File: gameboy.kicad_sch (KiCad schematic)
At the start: 0 parts

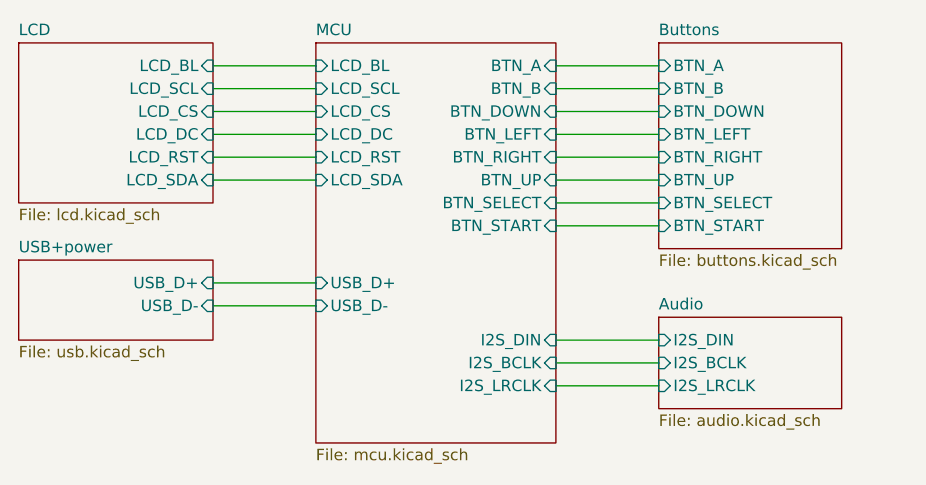
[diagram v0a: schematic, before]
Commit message: add amplifier mode selector, add drawing lcd
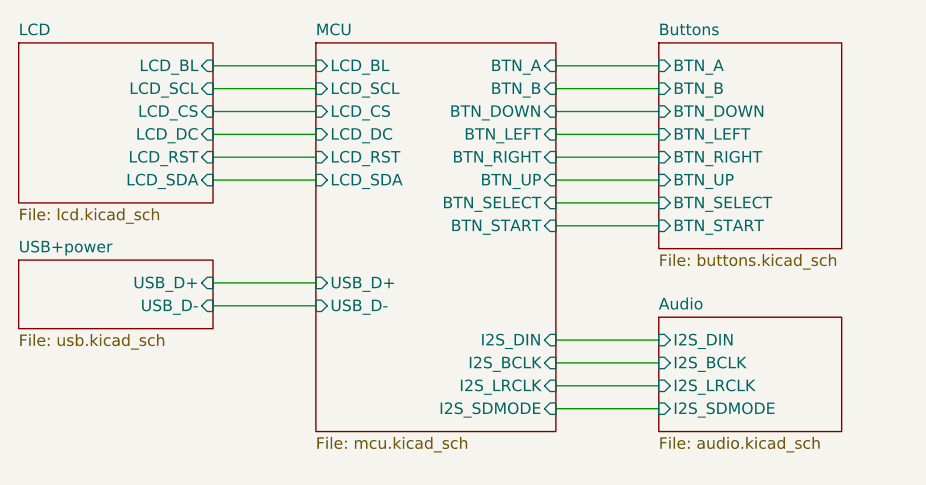
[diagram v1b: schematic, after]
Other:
- sheet Audio ports: added I2S_SDMODE; removed none
- sheet MCU ports: added I2S_SDMODE; removed none
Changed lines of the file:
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@@
+	(wire
+		(pts
+			(xy 167.64 99.06) (xy 179.07 99.06)
+		)
+		(stroke
+			(width 0)
+			(type default)
+		)
+	)
 	(wire
 		(pts
@@
 	(sheet
 		(at 140.97 58.42)
-		(size 26.67 44.45)
+		(size 26.67 43.18)
 		(exclude_from_sim no)
 		(in_bom yes)
@@
 		)
 		(property "Sheetfile" "mcu.kicad_sch"
-			(at 140.97 103.4546 0)
+			(at 140.97 102.1846 0)
 			(effects
 				(font
@@
 		(pin "I2S_LRCLK" input
 			(at 167.64 96.52 0)
+			(effects
+				(font
+					(size 1.27 1.27)
+				)
+				(justify right)
+			)
+		)
+		(pin "I2S_SDMODE" input
+			(at 167.64 99.06 0)
 			(effects
 				(font
@@
 	(sheet
 		(at 107.95 82.55)
-		(size 21.59 8.89)
+		(size 21.59 7.62)
 		(exclude_from_sim no)
 		(in_bom yes)
@@
 		)
 		(property "Sheetfile" "usb.kicad_sch"
-			(at 107.95 92.0246 0)
+			(at 107.95 90.7546 0)
 			(effects
 				(font
@@
 	(sheet
 		(at 179.07 88.9)
-		(size 20.32 10.16)
+		(size 20.32 12.7)
 		(exclude_from_sim no)
 		(in_bom yes)
@@
 		)
 		(property "Sheetfile" "audio.kicad_sch"
-			(at 179.07 99.6446 0)
+			(at 179.07 102.1846 0)
 			(effects
 				(font
@@
 			(effects
 				(font
+					(size 1.27 1.27)
+				)
+				(justify left)
+			)
+		)
+		(pin "I2S_SDMODE" input
+			(at 179.07 99.06 180)
+			(effects
+				(font

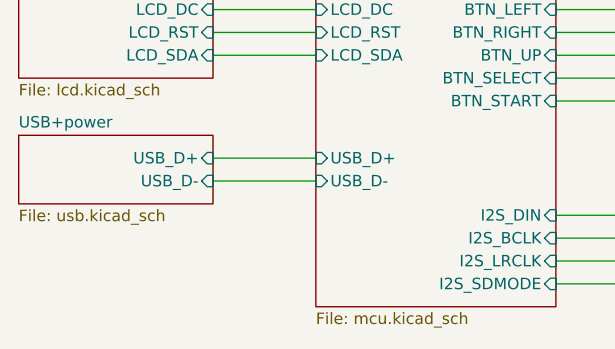
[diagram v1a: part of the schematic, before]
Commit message: add vibration motor
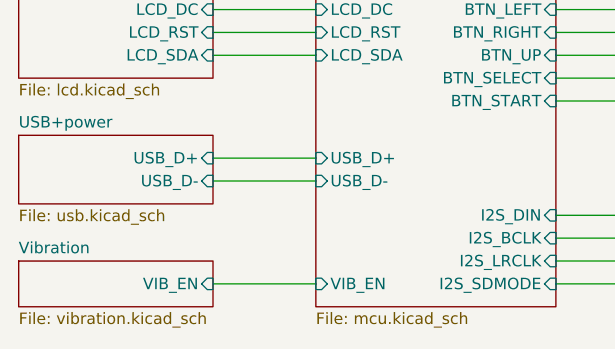
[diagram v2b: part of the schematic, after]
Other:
- added sheet Vibration (vibration.kicad_sch)
- sheet MCU ports: added VIB_EN; removed none
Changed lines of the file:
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@@
+	(wire
+		(pts
+			(xy 129.54 99.06) (xy 140.97 99.06)
+		)
+		(stroke
+			(width 0)
+			(type default)
+		)
+	)
 	(wire
 		(pts
@@
 			)
 		)
+		(pin "VIB_EN" input
+			(at 140.97 99.06 180)
+			(effects
+				(font
+					(size 1.27 1.27)
+				)
+				(justify left)
+			)
+		)
 		(instances
 			(project "gameboy"
@@
 				)
 			)
+		)
+	)
+	(sheet
+		(at 107.95 96.52)
+		(size 21.59 5.08)
+		(exclude_from_sim no)
+		(in_bom yes)
+		(on_board yes)
+		(dnp no)
+		(fields_autoplaced yes)
+		(stroke
+			(width 0.1524)
+			(type solid)
+		)
+		(fill
+			(color 0 0 0 0.0000)
+		)
+		(property "Sheetname" "Vibration"
+			(at 107.95 95.8084 0)
+			(effects
+				(font
+					(size 1.27 1.27)
+				)
+				(justify left bottom)
+			)
+		)
+		(property "Sheetfile" "vibration.kicad_sch"
+			(at 107.95 102.1846 0)
+			(effects
+				(font
+					(size 1.27 1.27)
+				)
+				(justify left top)
+			)
+		)
+		(pin "VIB_EN" input
+			(at 129.54 99.06 0)
+			(effects
+				(font
+					(size 1.27 1.27)
+				)
+				(justify right)
+			)
+		)
+		(instances
+			(project "gameboy"
+				(path "/f4643692-c319-40a7-82a2-3e775c0a417f"
+					(page "7")
+				)
+			)

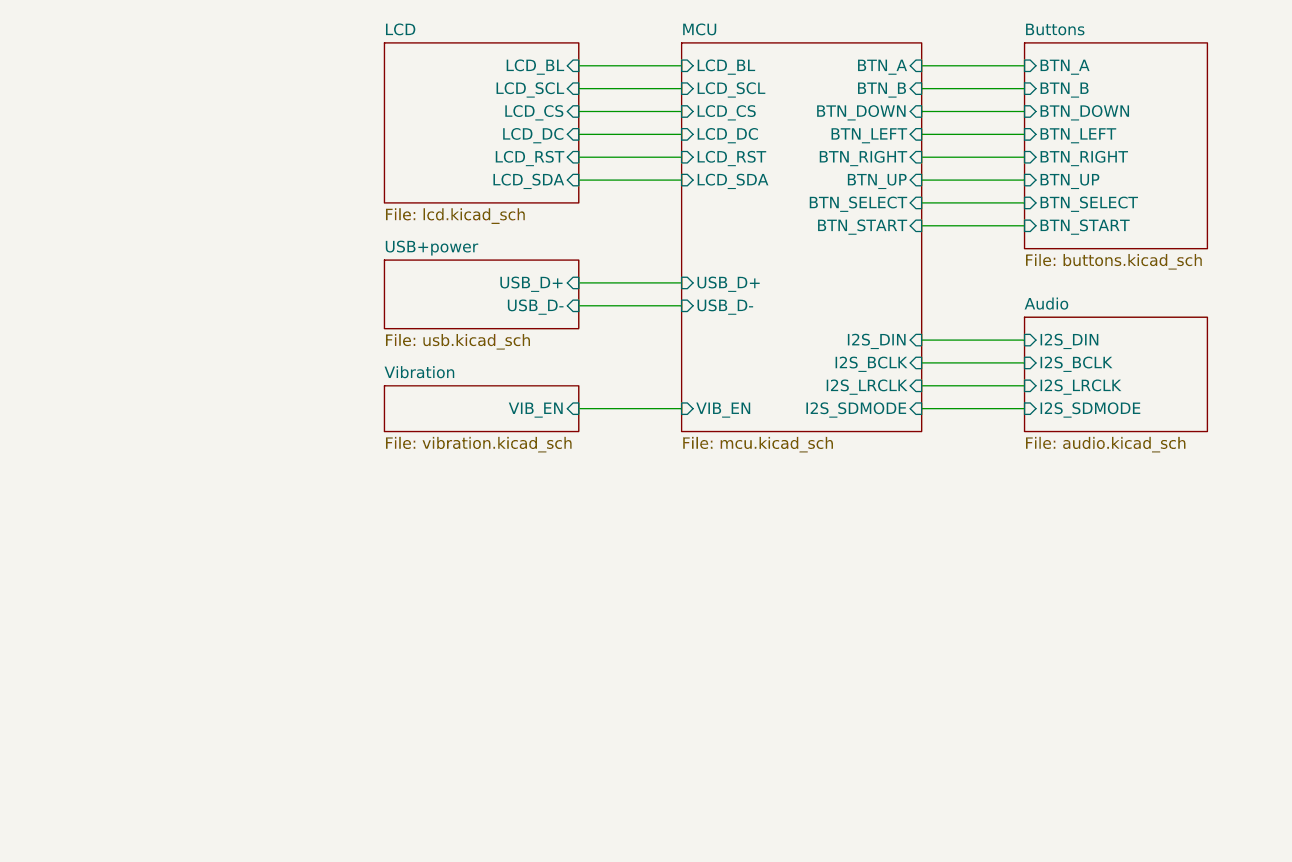
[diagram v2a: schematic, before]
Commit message: add SD card
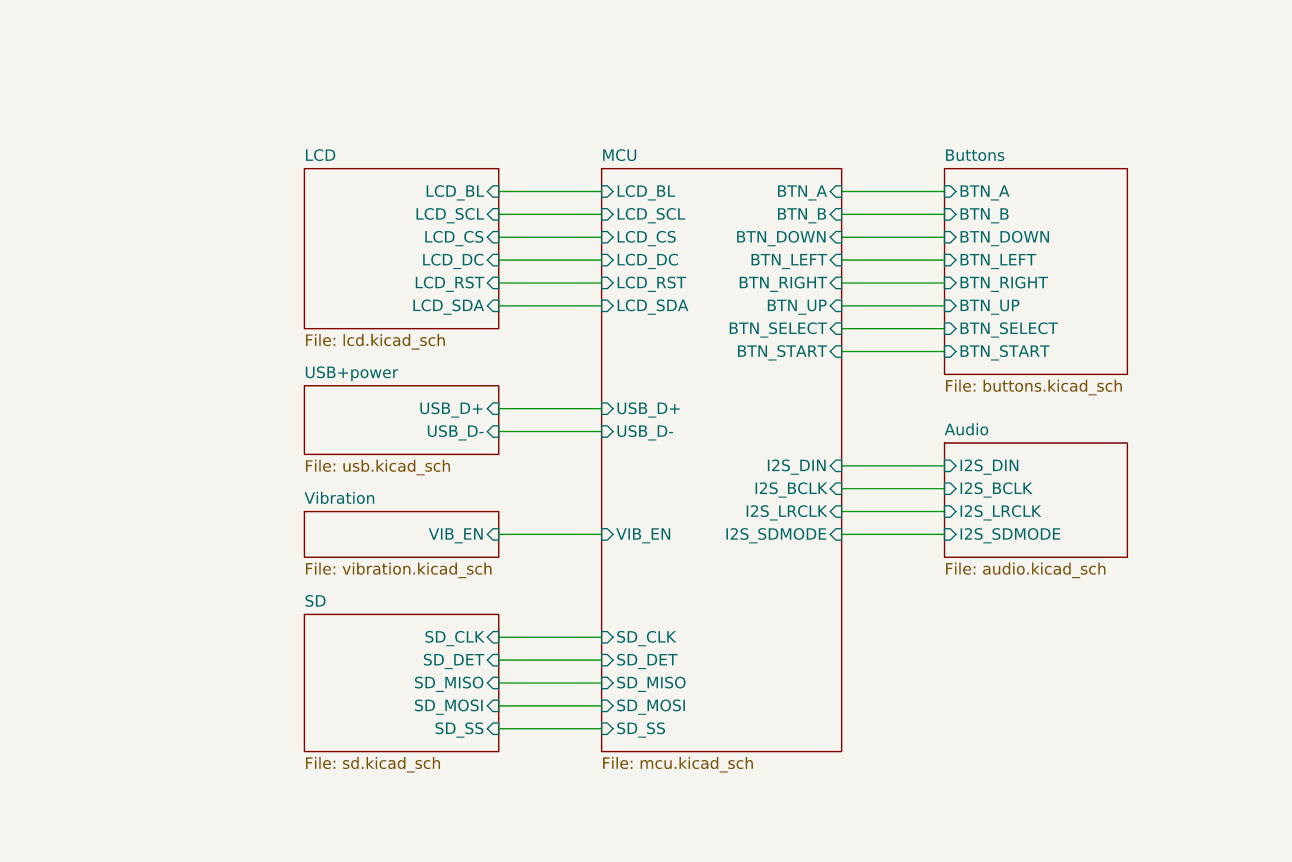
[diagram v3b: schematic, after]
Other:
- added sheet SD (sd.kicad_sch)
- sheet MCU ports: added SD_CLK, SD_DET, SD_MISO, SD_MOSI, SD_SS; removed none

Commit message: check with hardware manual, add comments, add mpns
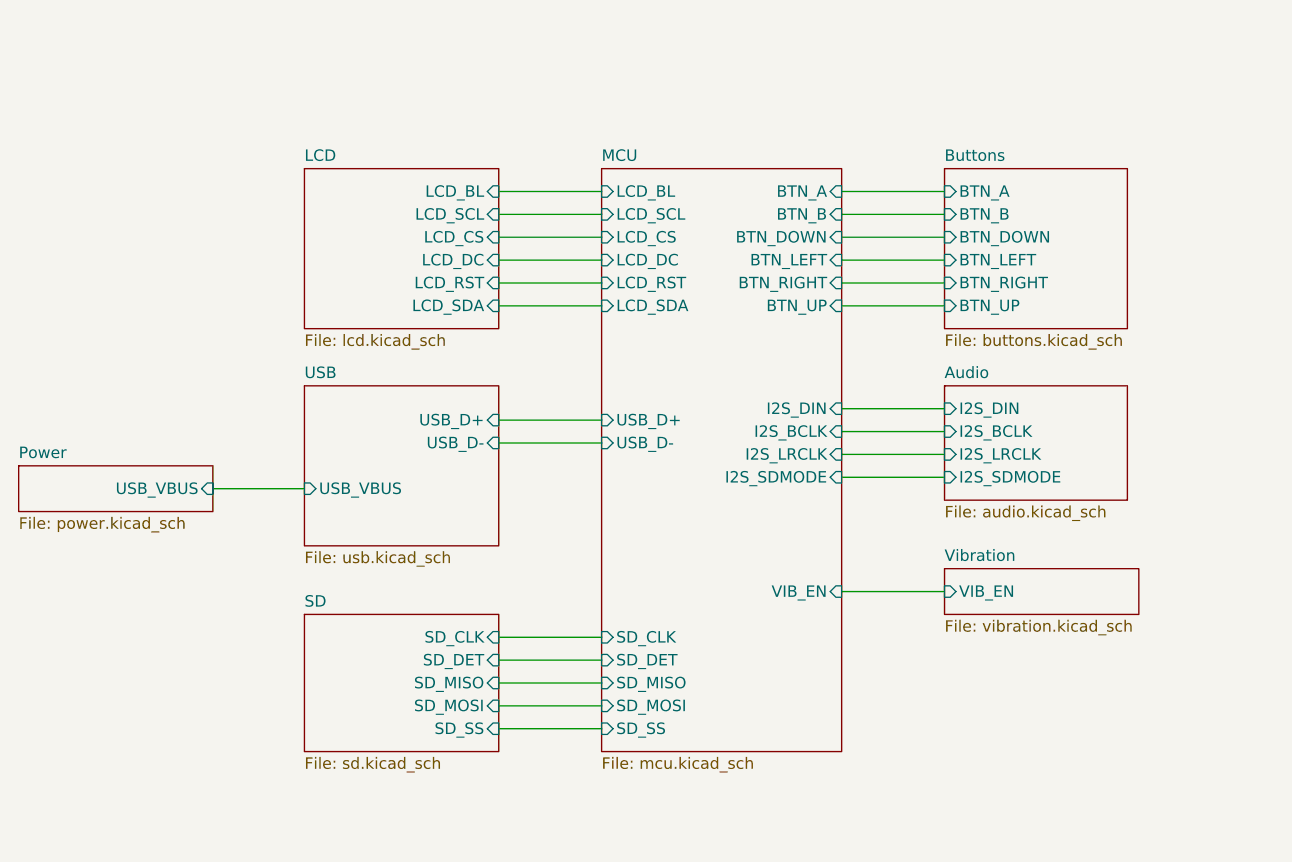
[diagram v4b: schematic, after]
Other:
- sheet USB+power renamed Power
- added sheet USB (usb.kicad_sch)
- sheet Buttons ports: added none; removed BTN_SELECT, BTN_START
- sheet MCU ports: added none; removed BTN_SELECT, BTN_START
- sheet Power: file usb.kicad_sch -> power.kicad_sch
- sheet Power ports: added USB_VBUS; removed USB_D+, USB_D-
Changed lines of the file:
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@@
 	(wire
 		(pts
-			(xy 120.65 113.03) (xy 132.08 113.03)
+			(xy 120.65 100.33) (xy 132.08 100.33)
+		)
+		(stroke
+			(width 0)
+			(type default)
+		)
+	)
+	(wire
+		(pts
+			(xy 170.18 119.38) (xy 158.75 119.38)
 		)
 		(stroke
@@
 	(wire
 		(pts
-			(xy 158.75 107.95) (xy 170.18 107.95)
-		)
-		(stroke
-			(width 0)
-			(type default)
-		)
-	)
-	(wire
-		(pts
-			(xy 158.75 105.41) (xy 170.18 105.41)
+			(xy 158.75 101.6) (xy 170.18 101.6)
+		)
+		(stroke
+			(width 0)
+			(type default)
+		)
+	)
+	(wire
+		(pts
+			(xy 158.75 99.06) (xy 170.18 99.06)
 		)
 		(stroke
@@
 	(wire
 		(pts
-			(xy 120.65 99.06) (xy 132.08 99.06)
-		)
-		(stroke
-			(width 0)
-			(type default)
-		)
-	)
-	(wire
-		(pts
 			(xy 158.75 82.55) (xy 170.18 82.55)
 		)
@@
 	(wire
 		(pts
-			(xy 158.75 110.49) (xy 170.18 110.49)
-		)
-		(stroke
-			(width 0)
-			(type default)
-		)
-	)
-	(wire
-		(pts
-			(xy 158.75 90.17) (xy 170.18 90.17)
+			(xy 158.75 104.14) (xy 170.18 104.14)
+		)
+		(stroke
+			(width 0)
+			(type default)
+		)
+	)
+	(wire
+		(pts
+			(xy 120.65 102.87) (xy 132.08 102.87)
 		)
 		(stroke
@@
 	(wire
 		(pts
-			(xy 158.75 113.03) (xy 170.18 113.03)
-		)
-		(stroke
-			(width 0)
-			(type default)
-		)
-	)
-	(wire
-		(pts
-			(xy 158.75 92.71) (xy 170.18 92.71)
+			(xy 158.75 106.68) (xy 170.18 106.68)
 		)
 		(stroke
@@
 	(wire
 		(pts
+			(xy 99.06 107.95) (xy 88.9 107.95)
+		)
+		(stroke
+			(width 0)
+			(type default)
+		)
+	)
+	(wire
+		(pts
 			(xy 120.65 132.08) (xy 132.08 132.08)
-		)
-		(stroke
-			(width 0)
-			(type default)
-		)
-	)
-	(wire
-		(pts
-			(xy 120.65 101.6) (xy 132.08 101.6)
 		)
 		(stroke
@@
 	(sheet
 		(at 170.18 72.39)
-		(size 20.32 22.86)
+		(size 20.32 17.78)
 		(exclude_from_sim no)
 		(in_bom yes)
@@
 		)
 		(property "Sheetfile" "buttons.kicad_sch"
-			(at 170.18 95.8346 0)
+			(at 170.18 90.7546 0)
 			(effects
 				(font
@@
 		(pin "BTN_RIGHT" input
 			(at 170.18 85.09 180)
-			(effects
-				(font
-					(size 1.27 1.27)
-				)
-				(justify left)
-			)
-		)
-		(pin "BTN_SELECT" input
-			(at 170.18 90.17 180)
-			(effects
-				(font
-					(size 1.27 1.27)
-				)
-				(justify left)
-			)
-		)
-		(pin "BTN_START" input
-			(at 170.18 92.71 180)
 			(effects
 				(font
@@
 		)
 		(pin "USB_D+" input
-			(at 132.08 99.06 180)
+			(at 132.08 100.33 180)
 			(effects
 				(font
@@
 		)
 		(pin "USB_D-" input
-			(at 132.08 101.6 180)
-			(effects
-				(font
-					(size 1.27 1.27)
-				)
-				(justify left)
-			)
-		)
-		(pin "BTN_SELECT" input
-			(at 158.75 90.17 0)
-			(effects
-				(font
-					(size 1.27 1.27)
-				)
-				(justify right)
-			)
-		)
-		(pin "BTN_START" input
-			(at 158.75 92.71 0)
-			(effects
-				(font
-					(size 1.27 1.27)
-				)
-				(justify right)
+			(at 132.08 102.87 180)
+			(effects
+				(font
+					(size 1.27 1.27)
+				)
+				(justify left)
 			)
 		)
 		(pin "I2S_BCLK" input
-			(at 158.75 107.95 0)
+			(at 158.75 101.6 0)
 			(effects
 				(font
@@
 		)
 		(pin "I2S_DIN" input
-			(at 158.75 105.41 0)
+			(at 158.75 99.06 0)
 			(effects
 				(font
@@
 		)
 		(pin "I2S_LRCLK" input
-			(at 158.75 110.49 0)
+			(at 158.75 104.14 0)
 			(effects
 				(font
@@
 		)
 		(pin "I2S_SDMODE" input
-			(at 158.75 113.03 0)
+			(at 158.75 106.68 0)
 			(effects
 				(font
@@
 		)
 		(pin "VIB_EN" input
-			(at 132.08 113.03 180)
-			(effects
-				(font
-					(size 1.27 1.27)
-				)
-				(justify left)
+			(at 158.75 119.38 0)
+			(effects
+				(font
+					(size 1.27 1.27)
+				)
+				(justify right)
 			)
 		)
@@
 	)
 	(sheet
-		(at 99.06 96.52)
-		(size 21.59 7.62)
+		(at 67.31 105.41)
+		(size 21.59 5.08)
 		(exclude_from_sim no)
 		(in_bom yes)
@@
 			(color 0 0 0 0.0000)
 		)
-		(property "Sheetname" "USB+power"
-			(at 99.06 95.8084 0)
+		(property "Sheetname" "Power"
+			(at 67.31 104.6984 0)
 			(effects
 				(font
@@
 			)
 		)
-		(property "Sheetfile" "usb.kicad_sch"
-			(at 99.06 104.7246 0)
+		(property "Sheetfile" "power.kicad_sch"
+			(at 67.31 111.0746 0)
 			(effects
 				(font
@@
 			)
 		)
-		(pin "USB_D+" input
-			(at 120.65 99.06 0)
-			(effects
-				(font
-					(size 1.27 1.27)
-				)
-				(justify right)
-			)
-		)
-		(pin "USB_D-" input
-			(at 120.65 101.6 0)
+		(pin "USB_VBUS" input
+			(at 88.9 107.95 0)
 			(effects
 				(font
@@
 	)
 	(sheet
-		(at 170.18 102.87)
+		(at 170.18 96.52)
 		(size 20.32 12.7)
 		(exclude_from_sim no)
@@
 		)
 		(property "Sheetname" "Audio"
-			(at 170.18 102.1584 0)
+			(at 170.18 95.8084 0)
 			(effects
 				(font
@@
 		)
 		(property "Sheetfile" "audio.kicad_sch"
-			(at 170.18 116.1546 0)
+			(at 170.18 109.8046 0)
 			(effects
 				(font
@@
 		)
 		(pin "I2S_BCLK" input
-			(at 170.18 107.95 180)
+			(at 170.18 101.6 180)
 			(effects
 				(font
@@
 		)
 		(pin "I2S_DIN" input
-			(at 170.18 105.41 180)
+			(at 170.18 99.06 180)
 			(effects
 				(font
@@
 		)
 		(pin "I2S_LRCLK" input
-			(at 170.18 110.49 180)
+			(at 170.18 104.14 180)
 			(effects
 				(font
@@
 		)
 		(pin "I2S_SDMODE" input
-			(at 170.18 113.03 180)
+			(at 170.18 106.68 180)
 			(effects
 				(font
@@
 				(path "/f4643692-c319-40a7-82a2-3e775c0a417f"
 					(page "6")
+				)
+			)
+		)
+	)
+	(sheet
+		(at 99.06 96.52)
+		(size 21.59 17.78)
+		(exclude_from_sim no)
+		(in_bom yes)
+		(on_board yes)
+		(dnp no)
+		(fields_autoplaced yes)
+		(stroke
+			(width 0.1524)
+			(type solid)
+		)
+		(fill
+			(color 0 0 0 0.0000)
+		)
+		(property "Sheetname" "USB"
+			(at 99.06 95.8084 0)
+			(effects
+				(font
+					(size 1.27 1.27)
+				)
+				(justify left bottom)
+			)
+		)
+		(property "Sheetfile" "usb.kicad_sch"
+			(at 99.06 114.8846 0)
+			(effects
+				(font
+					(size 1.27 1.27)
+				)
+				(justify left top)
+			)
+		)
+		(pin "USB_D+" input
+			(at 120.65 100.33 0)
+			(effects
+				(font
+					(size 1.27 1.27)
+				)
+				(justify right)
+			)
+		)
+		(pin "USB_D-" input
+			(at 120.65 102.87 0)
+			(effects
+				(font
+					(size 1.27 1.27)
+				)
+				(justify right)
+			)
+		)
+		(pin "USB_VBUS" input
+			(at 99.06 107.95 180)
+			(effects
+				(font
+					(size 1.27 1.27)
+				)
+				(justify left)
+			)
+		)
+		(instances
+			(project "gameboy"
+				(path "/f4643692-c319-40a7-82a2-3e775c0a417f"
+					(page "9")
 				)
 			)
@@
 	)
 	(sheet
-		(at 99.06 110.49)
+		(at 170.18 116.84)
 		(size 21.59 5.08)
 		(exclude_from_sim no)
@@
 		)
 		(property "Sheetname" "Vibration"
-			(at 99.06 109.7784 0)
+			(at 170.18 116.1284 0)
 			(effects
 				(font
@@
 		)
 		(property "Sheetfile" "vibration.kicad_sch"
-			(at 99.06 116.1546 0)
+			(at 170.18 122.5046 0)
 			(effects
 				(font
@@
 		)
 		(pin "VIB_EN" input
-			(at 120.65 113.03 0)
-			(effects
-				(font
-					(size 1.27 1.27)
-				)
-				(justify right)
-			)
-		)
+			(at 170.18 119.38 180)
+			(effects
+				(font
+					(size 1.27 1.27)
+				)
+				(justify left)
+			)
+		)
